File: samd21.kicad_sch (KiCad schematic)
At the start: 32 parts, among them IC1 SAMD21G18A, J1 USB_C, J2 DEBUG, SW5 RESET, U5 GD25Q32C

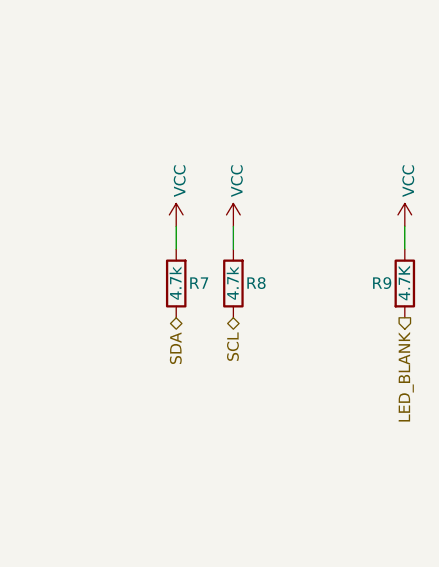
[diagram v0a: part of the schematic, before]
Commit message: Changed FETs to SOT-23 and buttons to something that is more boring
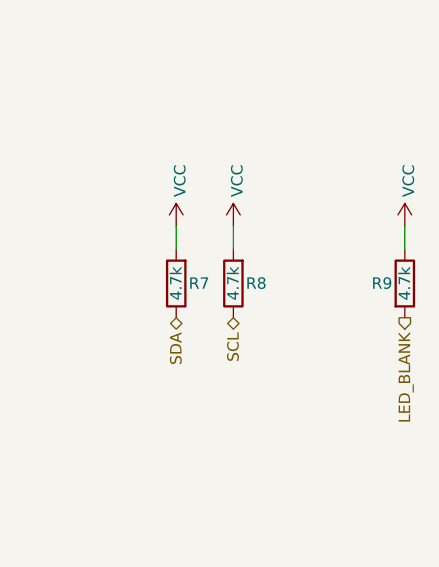
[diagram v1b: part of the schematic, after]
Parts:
- C5: LCSC (none) -> C15849
- C6: LCSC (none) -> C14663
- C7: LCSC (none) -> C19702
- D513: LCSC (none) -> C72043
- IC1: LCSC (none) -> C78624
- J1, J2, SW5, U5: LCSC (none) -> DNP
- R3, R4: LCSC (none) -> C23186
- R5: LCSC (none) -> C25804
- R6: LCSC (none) -> C21190
- R7, R8: LCSC (none) -> C23162
- R9: value 4.7K -> 4.7k; LCSC (none) -> C23162
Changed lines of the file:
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@@
+      (effects (font (size 1.27 1.27)) hide)
+    )
+    (property "LCSC" "C23186" (id 4) (at 60.96 40.64 0)
       (effects (font (size 1.27 1.27)) hide)
     )
@@
       (effects (font (size 1.27 1.27)) hide)
     )
+    (property "LCSC" "C23186" (id 4) (at 60.96 43.18 0)
+      (effects (font (size 1.27 1.27)) hide)
+    )
   )
   (symbol (lib_id "Device:R") (at 76.2 73.66 180) (unit 1)
@@
       (effects (font (size 1.27 1.27)) hide)
     )
+    (property "LCSC" "C21190" (id 4) (at 76.2 73.66 0)
+      (effects (font (size 1.27 1.27)) hide)
+    )
   )
   (symbol (lib_id "Device:R") (at 223.52 58.42 180) (unit 1)
@@
       (effects (font (size 1.27 1.27)) hide)
     )
+    (property "LCSC" "C25804" (id 4) (at 223.52 58.42 0)
+      (effects (font (size 1.27 1.27)) hide)
+    )
   )
   (symbol (lib_id "Device:R") (at 234.95 110.49 180) (unit 1)
@@
       (effects (font (size 1.27 1.27)) hide)
     )
+    (property "LCSC" "C23162" (id 4) (at 234.95 110.49 0)
+      (effects (font (size 1.27 1.27)) hide)
+    )
   )
   (symbol (lib_id "Device:R") (at 241.3 110.49 180) (unit 1)
@@
       (effects (font (size 1.27 1.27)) hide)
     )
+    (property "LCSC" "C23162" (id 4) (at 241.3 110.49 0)
+      (effects (font (size 1.27 1.27)) hide)
+    )
   )
   (symbol (lib_id "Device:R") (at 260.35 110.49 0) (unit 1)
     (in_bom yes) (on_board yes)
     (property "Reference" "R9" (id 0) (at 257.81 110.49 0))
-    (property "Value" "4.7K" (id 1) (at 260.35 110.49 90))
+    (property "Value" "4.7k" (id 1) (at 260.35 110.49 90))
     (property "Footprint" "Resistor_SMD:R_0603_1608Metric" (id 2) (at 258.572 110.49 90)
       (effects (font (size 1.27 1.27)) hide)
     )
     (property "Datasheet" "~" (id 3) (at 260.35 110.49 0)
+      (effects (font (size 1.27 1.27)) hide)
+    )
+    (property "LCSC" "C23162" (id 4) (at 260.35 110.49 0)
       (effects (font (size 1.27 1.27)) hide)
     )
@@
     )
     (property "Datasheet" "~" (id 3) (at 76.2 85.09 0)
+      (effects (font (size 1.27 1.27)) hide)
+    )
+    (property "LCSC" "C72043" (id 4) (at 76.2 85.09 0)
       (effects (font (size 1.27 1.27)) hide)
     )
@@
       (effects (font (size 1.27 1.27)) hide)
     )
+    (property "LCSC" "DNP" (id 4) (at 234.95 64.77 0)
+      (effects (font (size 1.27 1.27)) hide)
+    )
   )
   (symbol (lib_id "Device:C") (at 29.21 105.41 0) (unit 1)
@@
       (effects (font (size 1.27 1.27)) hide)
     )
+    (property "LCSC" "C14663" (id 4) (at 29.21 105.41 0)
+      (effects (font (size 1.27 1.27)) hide)
+    )
   )
   (symbol (lib_id "Device:C") (at 43.18 105.41 0) (unit 1)
@@
     )
     (property "Datasheet" "~" (id 3) (at 43.18 105.41 0)
+      (effects (font (size 1.27 1.27)) hide)
+    )
+    (property "LCSC" "C19702" (id 4) (at 43.18 105.41 0)
       (effects (font (size 1.27 1.27)) hide)
     )
@@
       (effects (font (size 1.27 1.27)) hide)
     )
+    (property "LCSC" "C15849" (id 4) (at 203.2 57.15 0)
+      (effects (font (size 1.27 1.27)) hide)
+    )
   )
   (symbol (lib_id "Connector:Conn_01x06_Female") (at 118.11 144.78 0) (unit 1)
@@
     )
     (property "Datasheet" "~" (id 3) (at 118.11 144.78 0)
+      (effects (font (size 1.27 1.27)) hide)
+    )
+    (property "LCSC" "DNP" (id 4) (at 118.11 144.78 0)
       (effects (font (size 1.27 1.27)) hide)
     )
@@
       (effects (font (size 1.27 1.27)) hide)
     )
+    (property "LCSC" "DNP" (id 4) (at 50.8 146.05 0)
+      (effects (font (size 1.27 1.27)) hide)
+    )
   )
   (symbol (lib_id "Connector:USB_C_Receptacle_USB2.0") (at 38.1 50.8 0) (unit 1)
@@
       (effects (font (size 1.27 1.27)) hide)
     )
+    (property "LCSC" "DNP" (id 4) (at 38.1 50.8 0)
+      (effects (font (size 1.27 1.27)) hide)
+    )
   )
   (symbol (lib_id "samd21g18a:SAMD21G18A") (at 143.51 77.47 0) (unit 1)
@@
       (effects (font (size 1.27 1.27)) hide)
     )
+    (property "LCSC" "C78624" (id 5) (at 143.51 77.47 0)
+      (effects (font (size 1.27 1.27)) hide)
+    )
